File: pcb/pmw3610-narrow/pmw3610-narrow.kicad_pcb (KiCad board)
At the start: 2 copper layers, 15 x 42 mm, 20 parts, among them J2 vik-module-connector, U1 MG6208T3-18, U2 PMW3610

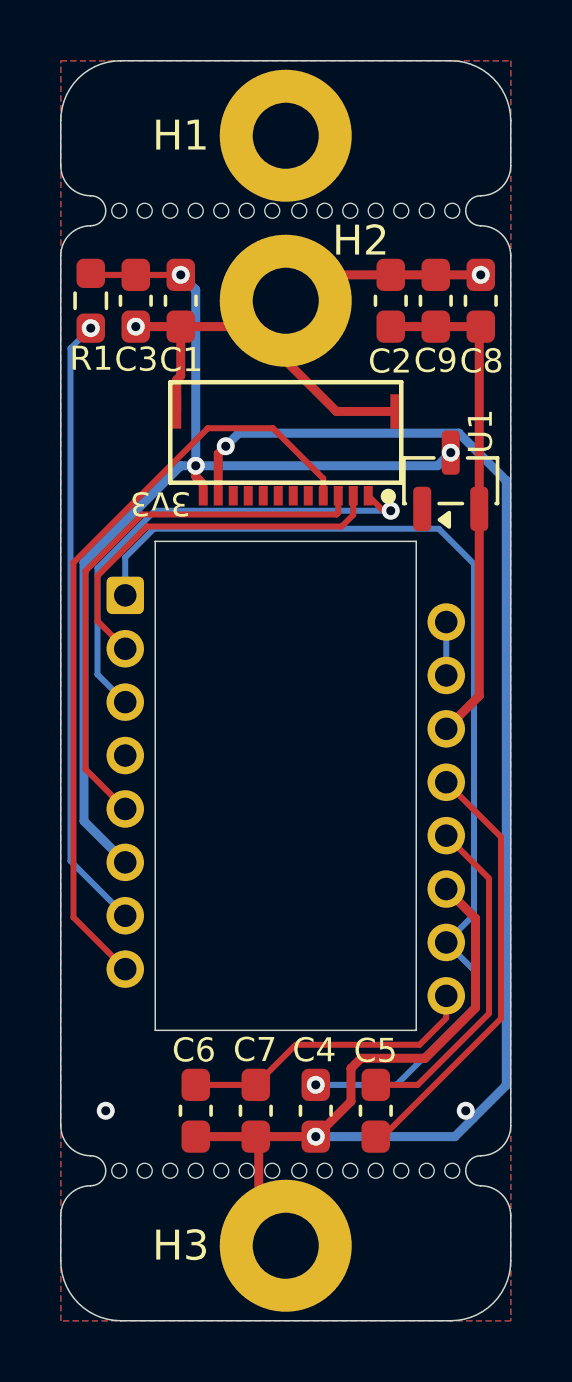
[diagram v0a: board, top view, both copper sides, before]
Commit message: Change voltage regulator on PMW3610-narrow.
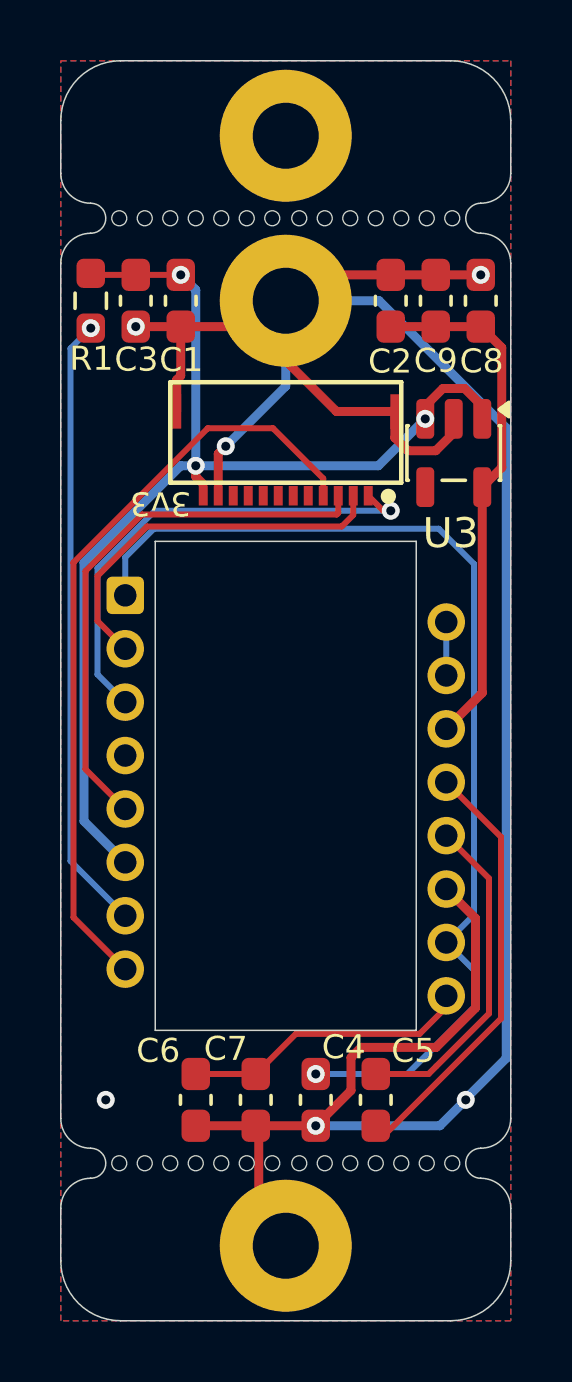
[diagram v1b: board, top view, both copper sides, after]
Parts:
- removed U1: MG6208T3-18, Package_TO_SOT_SMD:SOT-23
- added U3: TCR2EF19, Package_TO_SOT_SMD:SOT-23-5, F.Cu at (33.6, 33.1)
- C1: value 1u -> 0.1u
- moved C4 0.36 mm to (29.0, 54.6)
- moved C5 0.36 mm to (31.0, 54.6)
- moved C6 0.36 mm to (25.0, 54.6)
- moved C7 0.36 mm to (27.0, 54.6)
- moved REF** 0.25 mm to (31.0, 25.2)
- moved REF** 0.25 mm to (25.0, 56.8)
- moved REF** 0.25 mm to (25.0, 25.2)
- moved REF** 0.25 mm to (31.0, 56.8)
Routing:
- net GND: track 80.4 -> 89.7 mm
- net VCC: track 34.6 -> 37.5 mm
- net +1V9: track 16.9 -> 17.7 mm
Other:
- outline, holes or cut-outs redrawn

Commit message: Change passives to 0805 footprint.
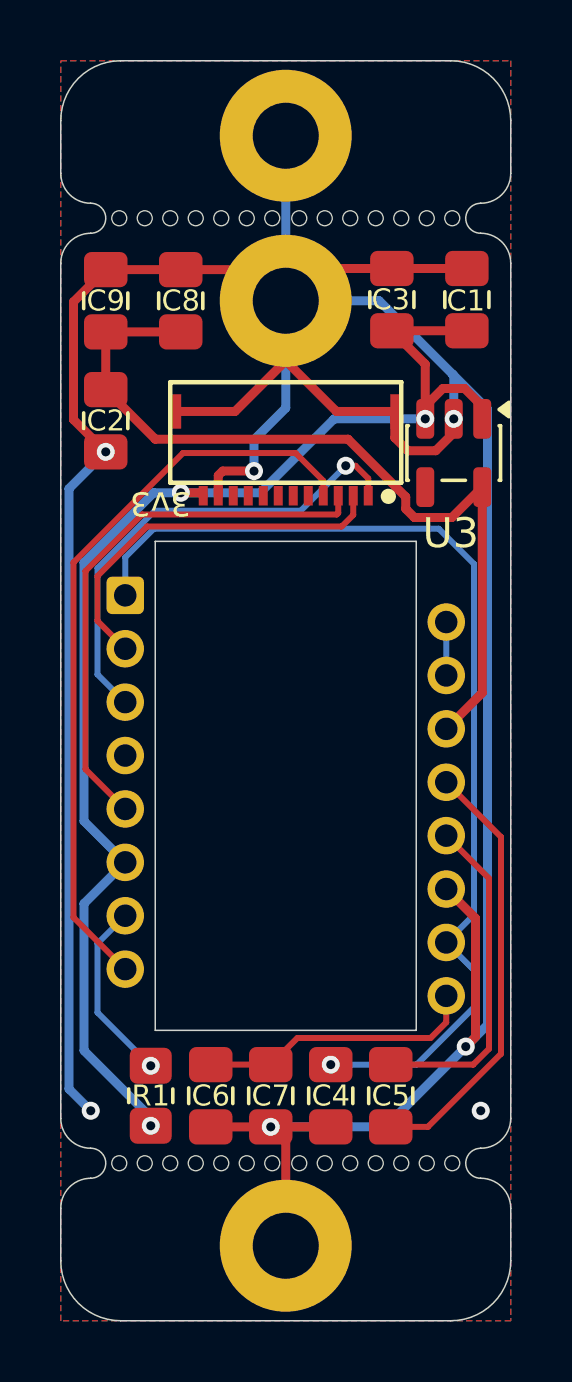
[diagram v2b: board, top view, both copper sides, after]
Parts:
- C1: value 0.1u -> 100n; footprint Capacitor_SMD:C_0603_1608Metric_Pad1.08x0.95mm_HandSolder -> Capacitor_SMD:C_0805_2012Metric_Pad1.18x1.45mm_HandSolder
- C2, C3, C4, C5, C6, C7, C8, C9: footprint Capacitor_SMD:C_0603_1608Metric_Pad1.08x0.95mm_HandSolder -> Capacitor_SMD:C_0805_2012Metric_Pad1.18x1.45mm_HandSolder
- R1: footprint Resistor_SMD:R_0603_1608Metric_Pad0.98x0.95mm_HandSolder -> Resistor_SMD:R_0805_2012Metric_Pad1.20x1.40mm_HandSolder
- moved R1 26.6 mm to (23.5, 54.5), turned to -90 degrees
- moved C9 11.0 mm to (22.0, 28.0)
- moved C2 10.3 mm to (22.0, 32.0), turned to -90 degrees
- moved C8 10.0 mm to (24.5, 28.0)
- moved C1 9.54 mm to (34.0, 28.0), turned to -90 degrees
- moved C3 8.54 mm to (31.5, 28.0), turned to 90 degrees
- moved C4 0.52 mm to (29.5, 54.5)
- moved C5 0.52 mm to (31.5, 54.5)
- moved C6 0.52 mm to (25.5, 54.5)
- moved C7 0.52 mm to (27.5, 54.5)
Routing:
- net GND: track 89.7 -> 123.4 mm, vias 6 -> 7
- net Net-(U2-NRESET): track 20.6 -> 6.12 mm
- net +1V9: track 17.7 -> 27.9 mm
- net VCC: track 37.5 -> 44.2 mm
- net MOTION: track 25.7 -> 25.0 mm
- net Net-(U2-+VCSEL): track 35.5 -> 34.9 mm
